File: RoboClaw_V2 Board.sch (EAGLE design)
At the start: 7 parts

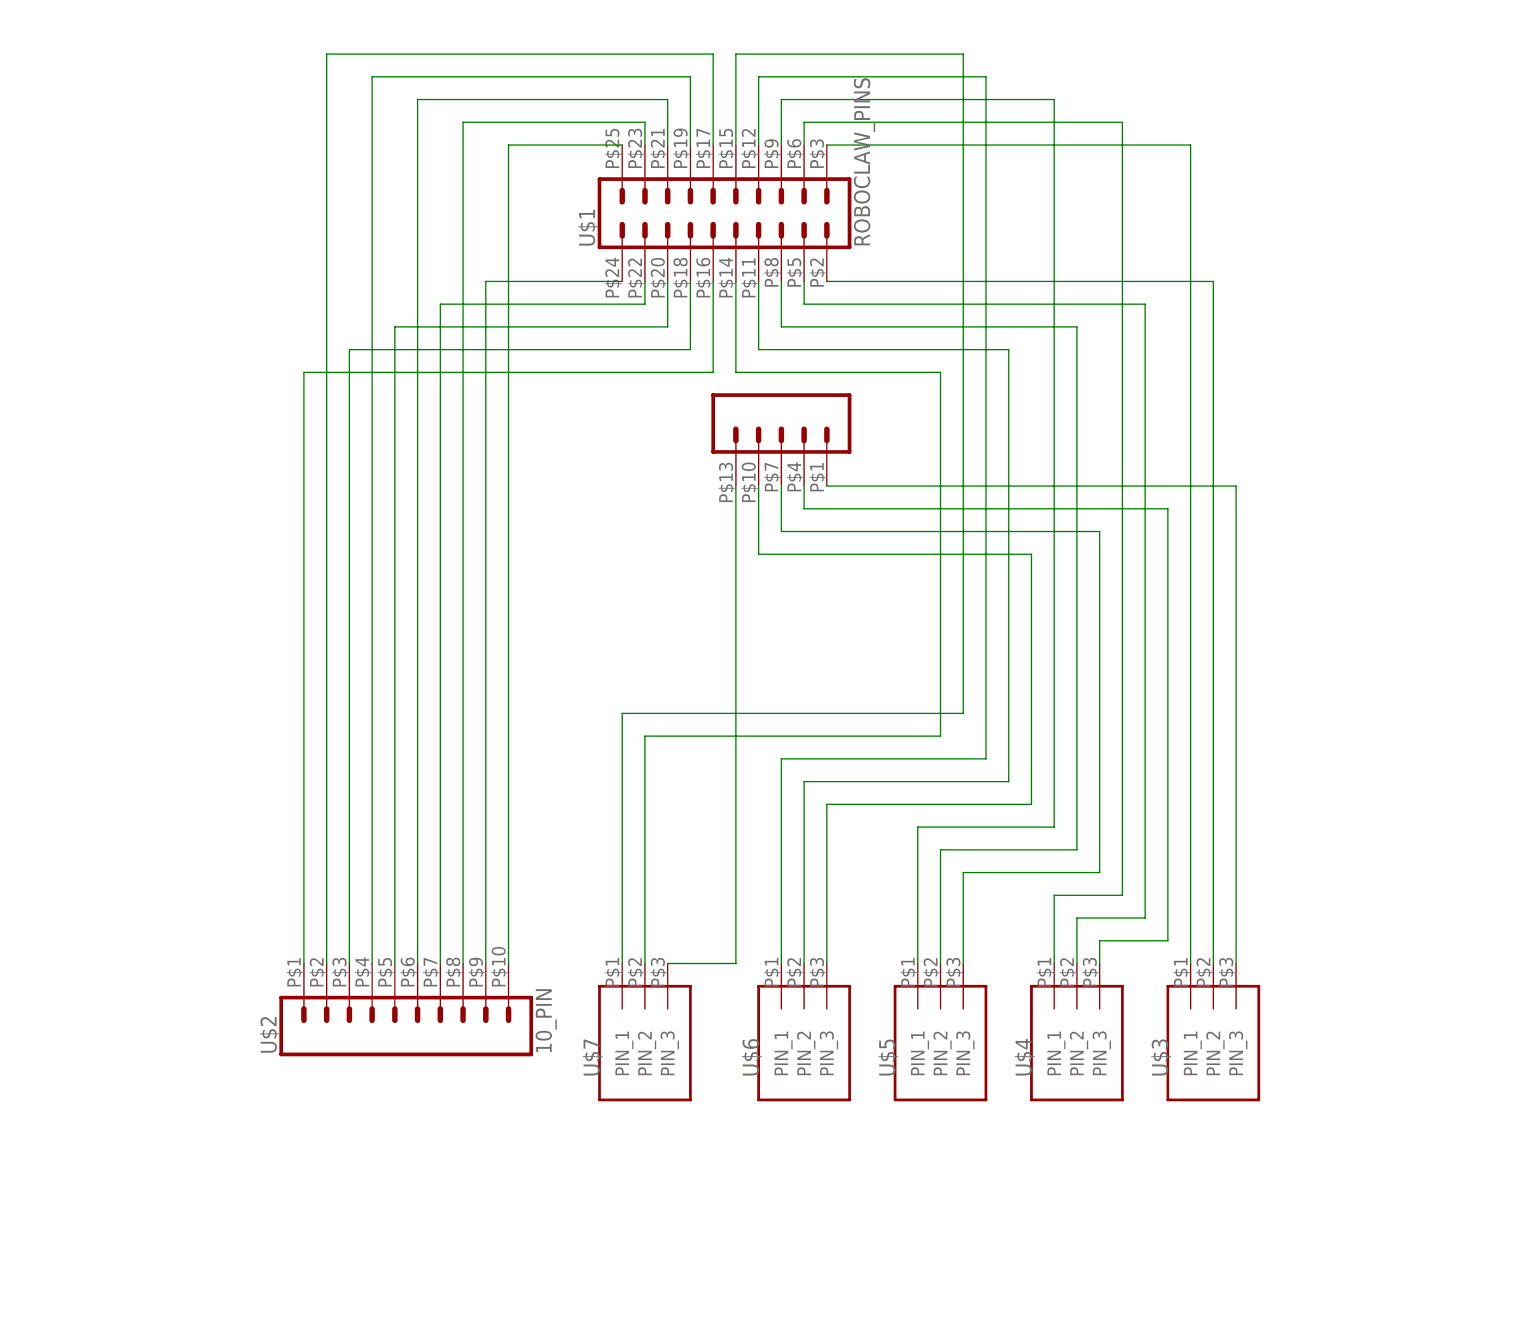
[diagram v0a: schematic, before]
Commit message: Added in some new connectors in the schematic and resized board
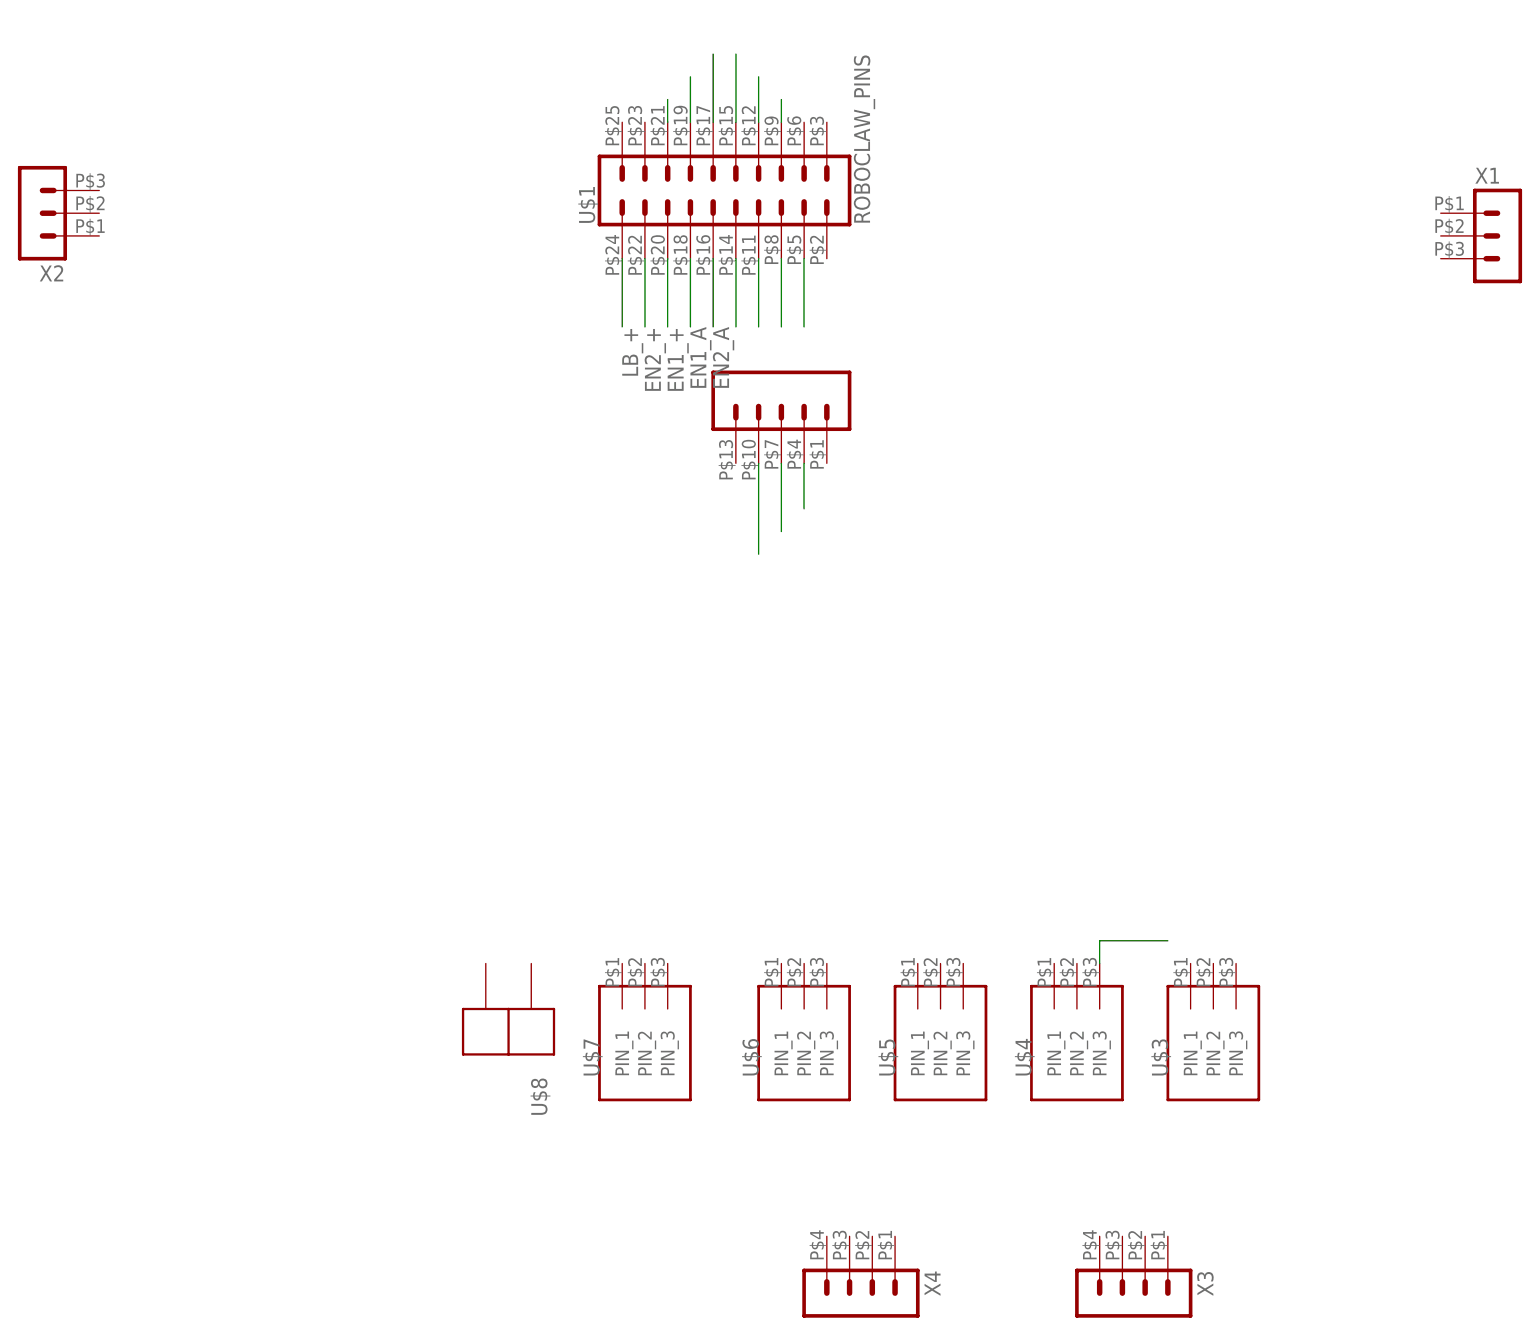
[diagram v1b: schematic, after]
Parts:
- removed U$2: 10_PIN, Screw Blocks:10_PIN
- added U$8: (no value), 000_CustomPartsMaster:2PIN-HEADERANDERSON_RIGHTANGLE
- added X1, X2: (no value), con-molex-micro-fit-3_0:HEADER_POS3_43650-0300
- added X3, X4: (no value), con-molex-micro-fit-3_0:HEADER_POS4_43045-0401
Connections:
- removed net N$10: U$1.PIN_12, U$6.PIN_1
- removed net N$13: U$1.PIN_15, U$7.PIN_1
- removed net N$14: U$1.PIN_14, U$7.PIN_2
- removed net N$16: U$1.PIN_18, U$2.PIN_3
- removed net N$17: U$1.PIN_21, U$2.PIN_6
- removed net N$18: U$1.PIN_20, U$2.PIN_5
- removed net N$19: U$1.PIN_23, U$2.PIN_8
- removed net N$20: U$1.PIN_22, U$2.PIN_7
- removed net N$21: U$1.PIN_24, U$2.PIN_9
- removed net N$22: U$1.PIN_25, U$2.PIN_10
- removed net N$24: U$1.PIN_17, U$2.PIN_2
- removed net N$25: U$1.PIN_16, U$2.PIN_1
- removed net N$26: U$1.PIN_19, U$2.PIN_4
- removed net N$28: U$1.PIN_13, U$7.PIN_3
- removed net N$4: U$1.PIN_6, U$4.PIN_1
- removed net N$5: U$1.PIN_5, U$4.PIN_2
- new net EN1_+: U$1.PIN_20
- new net EN1_A: U$1.PIN_18
- new net EN2_+: U$1.PIN_22
- new net EN2_A: U$1.PIN_16
- new net LB_+: U$1.PIN_24
- new net N$29: U$1.PIN_12
- new net N$30: U$1.PIN_11
- new net N$31: U$1.PIN_10
- new net N$32: U$1.PIN_15
- new net N$33: U$1.PIN_14
- net N$1: now also U$1.PIN_17; no longer U$1.PIN_1, U$3.PIN_3
- net N$11: now also U$1.PIN_5; no longer U$1.PIN_11, U$6.PIN_2
- net N$12: now also U$1.PIN_4; no longer U$1.PIN_10, U$6.PIN_3
- net N$2: now also U$1.PIN_19; no longer U$1.PIN_2, U$3.PIN_2
- net N$3: now also U$1.PIN_21; no longer U$1.PIN_3, U$3.PIN_1
- net N$6: no longer U$1.PIN_4
- net N$7: no longer U$5.PIN_1
- net N$8: no longer U$5.PIN_2
- net N$9: no longer U$5.PIN_3
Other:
- moved on the sheet: U$1

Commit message: Wired the schematic. Placed and wired the board. First Draft
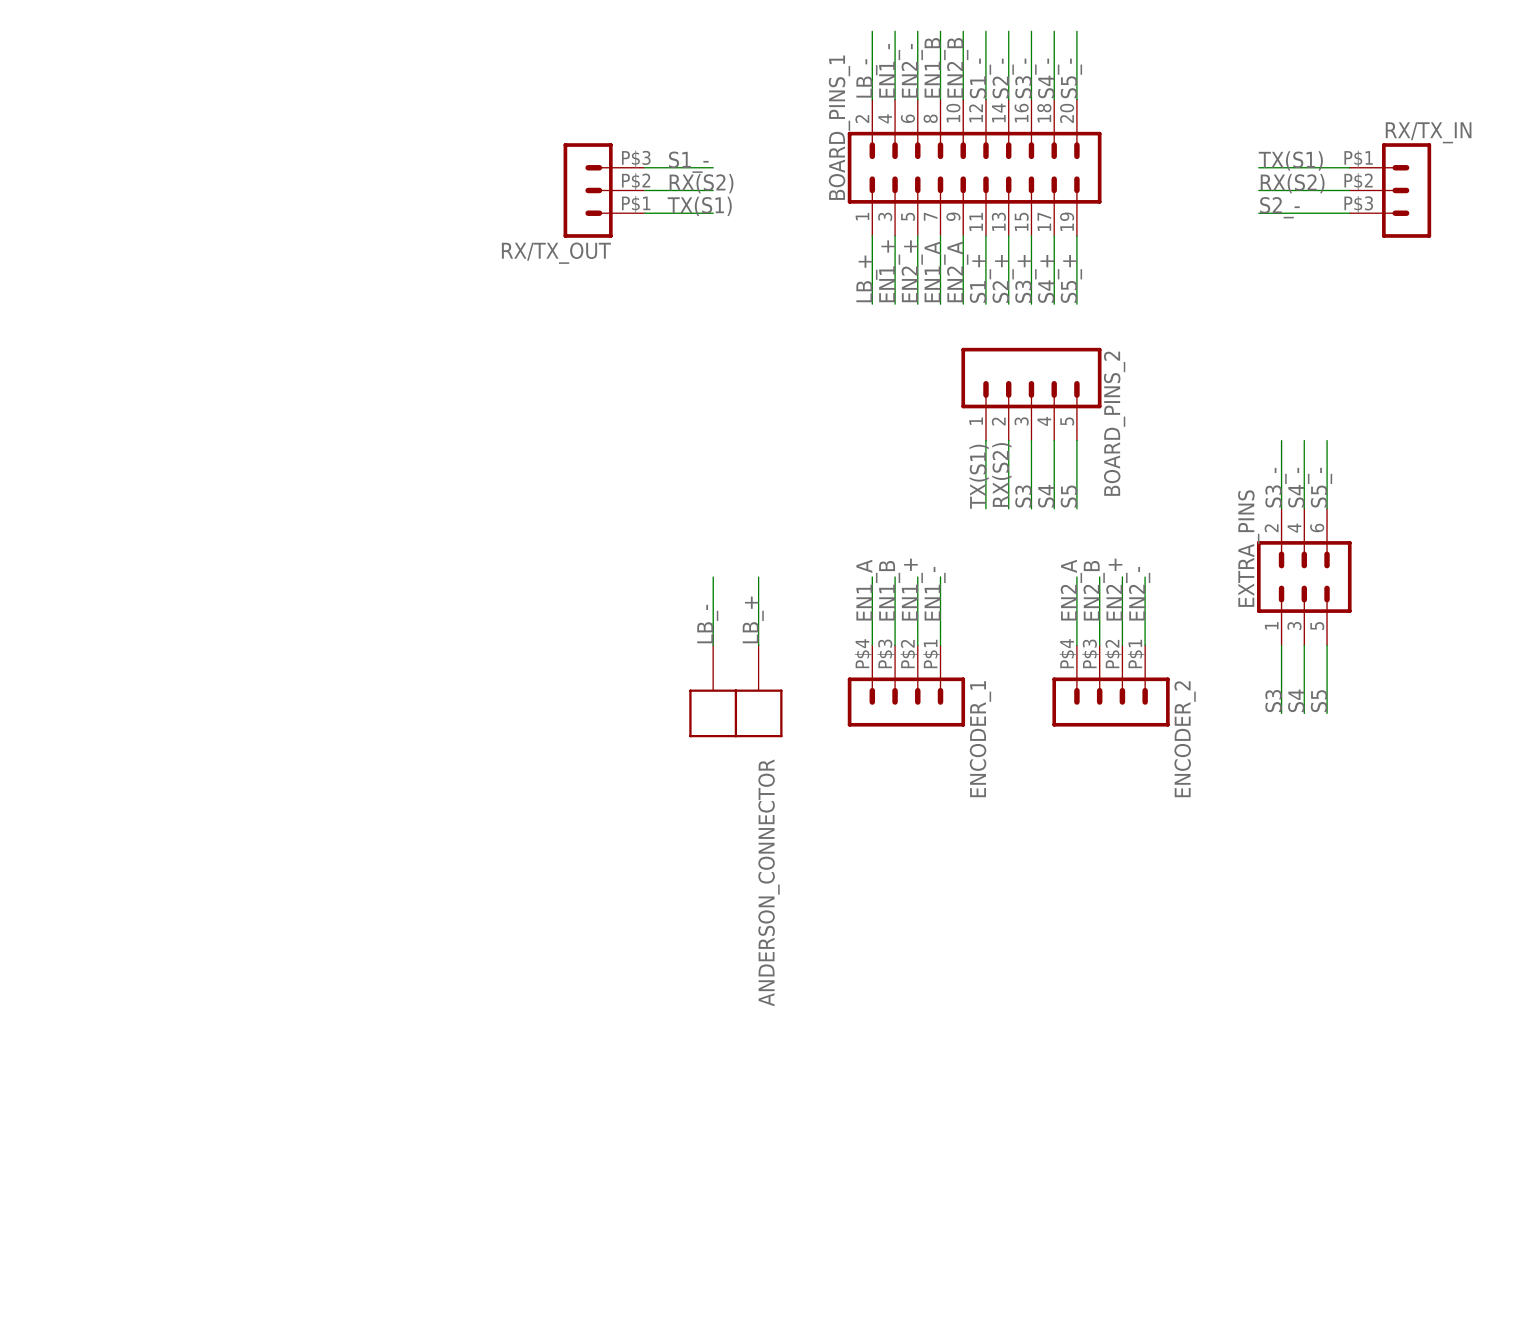
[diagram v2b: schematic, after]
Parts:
- removed U$1: ROBOCLAW_PINS, Screw Blocks:ROBOCLAW_PINS
- removed U$3, U$4, U$5, U$6, U$7: (no value), Screw Blocks:3_PIN
- removed U$8: (no value), 000_CustomPartsMaster:2PIN-HEADERANDERSON_RIGHTANGLE
- removed X1, X2: (no value), con-molex-micro-fit-3_0:HEADER_POS3_43650-0300
- removed X3, X4: (no value), con-molex-micro-fit-3_0:HEADER_POS4_43045-0401
- added ANDERSON_CONNECTOR: (no value), 000_CustomPartsMaster:2PIN-HEADERANDERSON_RIGHTANGLE
- added BOARD_PINS_1: (no value), SparkFun-Connectors:CONN_10X2NOSILK
- added BOARD_PINS_2: (no value), SparkFun-Connectors:CONN_05NO_SILK
- added ENCODER_1, ENCODER_2: (no value), con-molex-micro-fit-3_0:HEADER_POS4_43045-0401
- added EXTRA_PINS: (no value), SparkFun-Connectors:CONN_03X2NO_SILK
- added RX/TX_IN, RX/TX_OUT: (no value), con-molex-micro-fit-3_0:HEADER_POS3_43650-0300
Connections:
- removed net N$1: U$1.PIN_17
- removed net N$11: U$1.PIN_5
- removed net N$12: U$1.PIN_4
- removed net N$2: U$1.PIN_19
- removed net N$29: U$1.PIN_12
- removed net N$3: U$1.PIN_21
- removed net N$30: U$1.PIN_11
- removed net N$31: U$1.PIN_10
- removed net N$32: U$1.PIN_15
- removed net N$33: U$1.PIN_14
- removed net N$6: U$4.PIN_3
- removed net N$7: U$1.PIN_9
- removed net N$8: U$1.PIN_8
- removed net N$9: U$1.PIN_7
- new net EN1_-: BOARD_PINS_1.4, ENCODER_1.1
- new net EN1_B: BOARD_PINS_1.8, ENCODER_1.3
- new net EN2_-: BOARD_PINS_1.6, ENCODER_2.1
- new net EN2_B: BOARD_PINS_1.10, ENCODER_2.3
- new net LB_-: ANDERSON_CONNECTOR.P$2, BOARD_PINS_1.2
- new net RX(S2): BOARD_PINS_2.2, RX/TX_IN.2, RX/TX_OUT.2
- new net S1_+: BOARD_PINS_1.11
- new net S1_-: BOARD_PINS_1.12, RX/TX_OUT.3
- new net S2_+: BOARD_PINS_1.13
- new net S2_-: BOARD_PINS_1.14, RX/TX_IN.3
- new net S3: BOARD_PINS_2.3, EXTRA_PINS.1
- new net S3_+: BOARD_PINS_1.15
- new net S3_-: BOARD_PINS_1.16, EXTRA_PINS.2
- new net S4: BOARD_PINS_2.4, EXTRA_PINS.3
- new net S4_+: BOARD_PINS_1.17
- new net S4_-: BOARD_PINS_1.18, EXTRA_PINS.4
- new net S5: BOARD_PINS_2.5, EXTRA_PINS.5
- new net S5_+: BOARD_PINS_1.19
- new net S5_-: BOARD_PINS_1.20, EXTRA_PINS.6
- new net TX(S1): BOARD_PINS_2.1, RX/TX_IN.1, RX/TX_OUT.1
- net EN1_+: now also BOARD_PINS_1.3, ENCODER_1.2; no longer U$1.PIN_20
- net EN1_A: now also BOARD_PINS_1.7, ENCODER_1.4; no longer U$1.PIN_18
- net EN2_+: now also BOARD_PINS_1.5, ENCODER_2.2; no longer U$1.PIN_22
- net EN2_A: now also BOARD_PINS_1.9, ENCODER_2.4; no longer U$1.PIN_16
- net LB_+: now also ANDERSON_CONNECTOR.P$1, BOARD_PINS_1.1; no longer U$1.PIN_24
